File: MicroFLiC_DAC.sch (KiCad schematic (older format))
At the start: 35 parts, among them P1 2x4_MicroMaTch, P2 2x4_HEADER, P3 SMA, P4 SMA, P5 SMA, P6 SMA, P7 1x2_HEADER, P8 1x2_SOCKET, U1 DAC8734

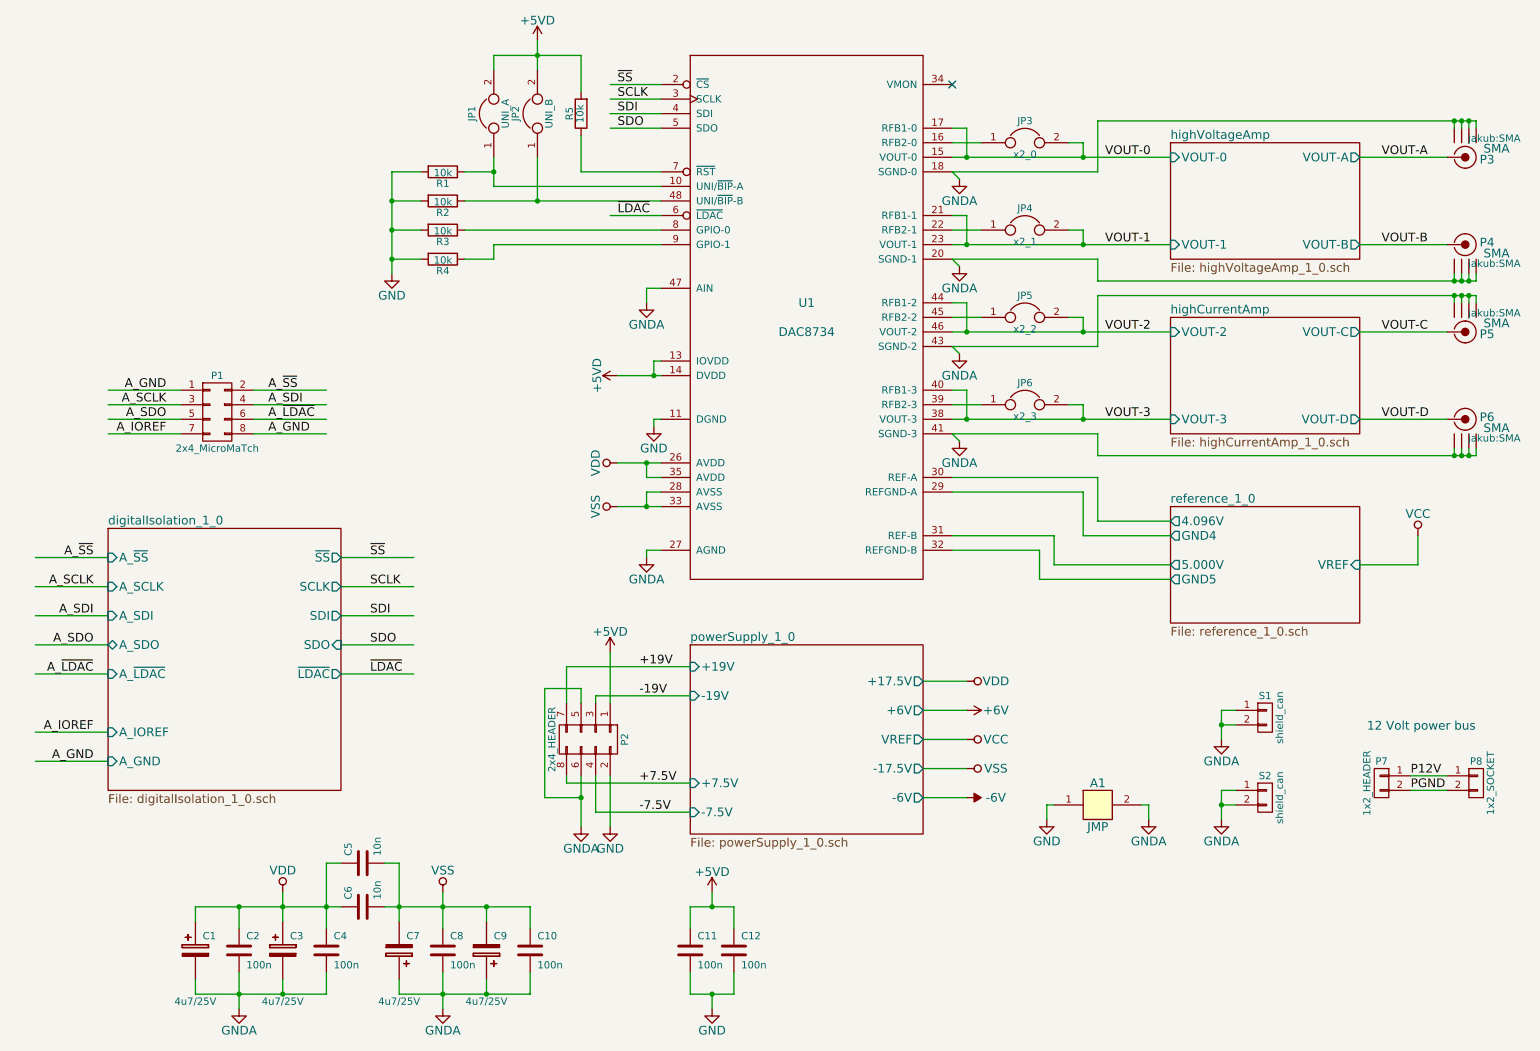
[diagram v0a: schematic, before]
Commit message: Updated all part descriptions
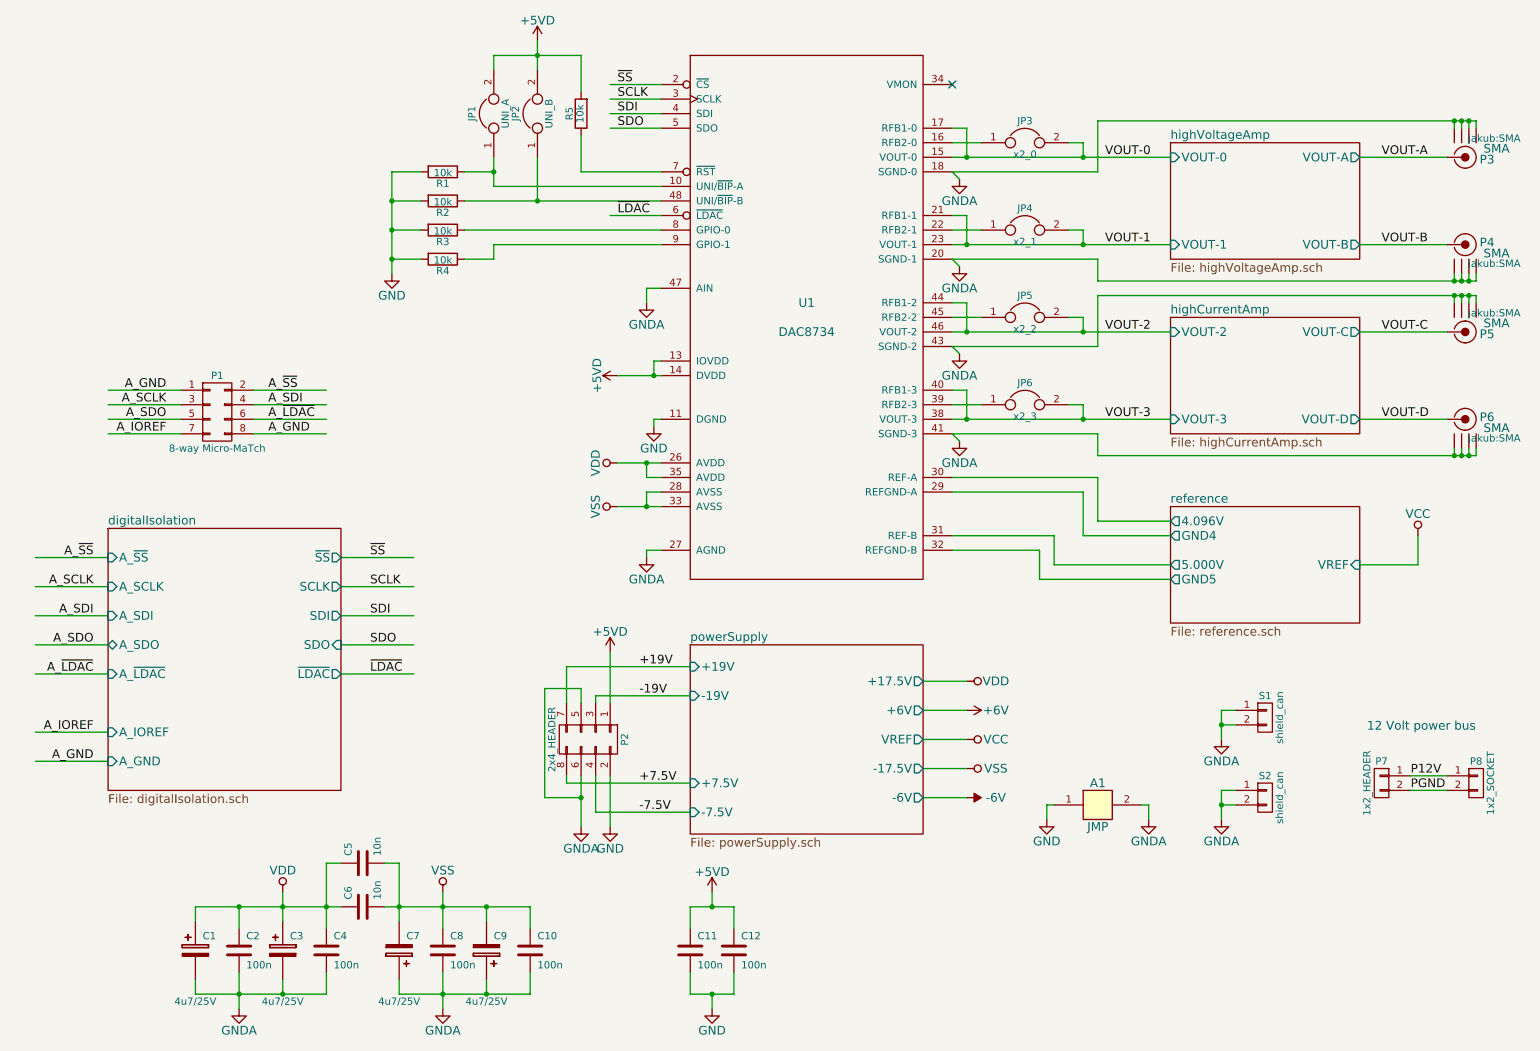
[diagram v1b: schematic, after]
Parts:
- C1, C3, C7, C9: Alt. Order Code (none) -> 74-TR3B475K025C0700; Alt. Supplier (none) -> Mouser; Note (none) -> 4.7μF/25V/0.7Ω ESR case B tantalum capacitor; Package (none) -> case B; Supplier (none) -> Farnell
- C10, C11, C12, C2, C4, C8: Alt. Order Code (none) -> 710-885012206095; Alt. Supplier (none) -> Mouser; Note (none) -> 100nF/50V X7R 0603 ceramic capacitor; Package (none) -> 0603; Supplier (none) -> Farnell
- C5, C6: Alt. Order Code (none) -> 77-VJ0603Y103KXACBC; Alt. Supplier (none) -> Mouser; Note (none) -> 10nF/100V X7R 0603 ceramic capacitor; Package (none) -> 0603; Supplier (none) -> Farnell
- P1: value 2x4_MicroMaTch -> 8-way Micro-MaTch; Alt. Order Code (none) -> 571-7-188275-8; Alt. Supplier (none) -> Mouser; Note (none) -> 8-way SMD Micro-MaTch connector; Package (none) -> Micro-MaTch SMD; Supplier (none) -> Farnell
- P2: Alt. Order Code (none) -> 710-61300421121; Alt. Supplier (none) -> Mouser; Note (none) -> 2x4 header strip; Package (none) -> DIL-8; Supplier (none) -> Farnell
- P3, P4, P5, P6: Alt. Order Code (none) -> 538-73251-2200; Alt. Supplier (none) -> Mouser; Note (none) -> R/A SMA jack; Package (none) -> SMA; Supplier (none) -> Farnell
- P7: Alt. Order Code (none) -> 855-M20-9990245; Alt. Supplier (none) -> Mouser; Note (none) -> 1x2 header strip; Package (none) -> SIL-2; Supplier (none) -> Farnell
- P8: Alt. Order Code (none) -> ESQ-102-33-G-S; Alt. Supplier (none) -> Samtec; Note (none) -> 1x2 ESQ series elevated socket strip; Package (none) -> SIL-2; Part Number SSA-102-S-G -> ESQ-102-33-G-S; Supplier (none) -> Farnell
- R1, R2, R3, R4, R5: Alt. Order Code (none) -> 71-CRCW0805-10K-E3; Alt. Supplier (none) -> Mouser; Note (none) -> 10kΩ/1% 0805 resistor; Package (none) -> 0805; Supplier (none) -> Farnell
- S1, S2: Alt. Order Code (none) -> MS323-20; Alt. Supplier (none) -> Masach; Note (none) -> Two-piece EMI shielding can; Order Code 826-6788 (RS Components) -> 826-6788; Package (none) -> Can; Supplier (none) -> RS Components
- U1: Alt. Order Code (none) -> 595-DAC8734SPFB; Alt. Supplier (none) -> Mouser; Note (none) -> Quad 16-bit DAC; Package (none) -> TQFP-48; Supplier (none) -> Farnell

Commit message: Fixed P8 socket Farnell code
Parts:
- P8: Order Code 1668221 -> 1927389
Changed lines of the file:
@@
 F 6 "SIL-2" H 10700 5850 60  0001 C CNN "Package"
 F 7 "Farnell" H 10700 5850 60  0001 C CNN "Supplier"
-F 8 "1668221" H 10700 5850 60  0001 C CNN "Order Code"
+F 8 "1927389" H 10700 5850 60  0001 C CNN "Order Code"
 F 9 "Samtec" H 10700 5850 60  0001 C CNN "Alt. Supplier"
 F 10 "ESQ-102-33-G-S" H 10700 5850 60  0001 C CNN "Alt. Order Code"

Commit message: Fixed P2 socket Farnell code
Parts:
- P2: Alt. Order Code 710-61300421121 -> 855-M20-9980446; Manufacturer Wurth Elektronik -> Harwin; Order Code 2356130 -> 1022233; Part Number 61300421121 -> M20-9980446
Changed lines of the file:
@@
 F 2 "Pin_Headers:Pin_Header_Straight_2x04" H 4600 4350 60  0001 C CNN
 F 3 "" H 4600 4350 60  0000 C CNN
-F 4 "61300421121" H 4600 5550 60  0001 C CNN "Part Number"
-F 5 "Wurth Elektronik" H 4600 5550 60  0001 C CNN "Manufacturer"
+F 4 "M20-9980446" H 4600 5550 60  0001 C CNN "Part Number"
+F 5 "Harwin" H 4600 5550 60  0001 C CNN "Manufacturer"
 F 6 "DIL-8" H 4600 5550 60  0001 C CNN "Package"
 F 7 "Farnell" H 4600 5550 60  0001 C CNN "Supplier"
-F 8 "2356130" H 4600 5550 60  0001 C CNN "Order Code"
+F 8 "1022233" H 4600 5550 60  0001 C CNN "Order Code"
 F 9 "Mouser" H 4600 5550 60  0001 C CNN "Alt. Supplier"
-F 10 "710-61300421121" H 4600 5550 60  0001 C CNN "Alt. Order Code"
+F 10 "855-M20-9980446" H 4600 5550 60  0001 C CNN "Alt. Order Code"
 F 11 "2x4 header strip" H 4600 5550 60  0001 C CNN "Note"
 	1    4600 5550

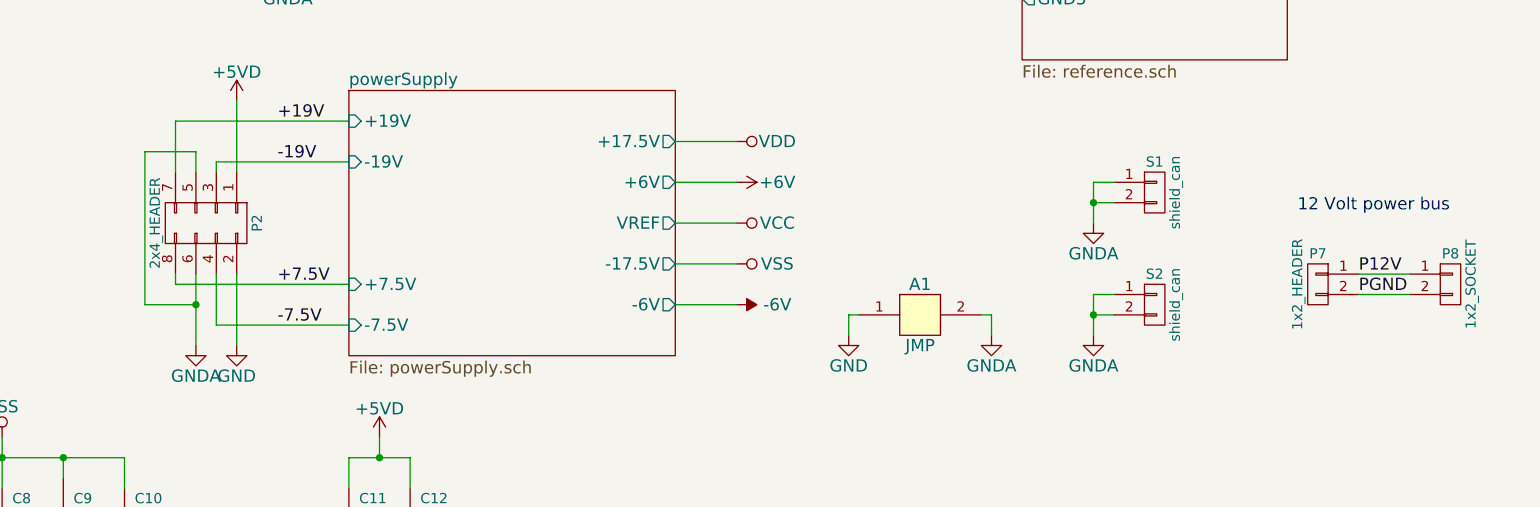
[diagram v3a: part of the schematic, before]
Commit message: Fixed connector descriptions
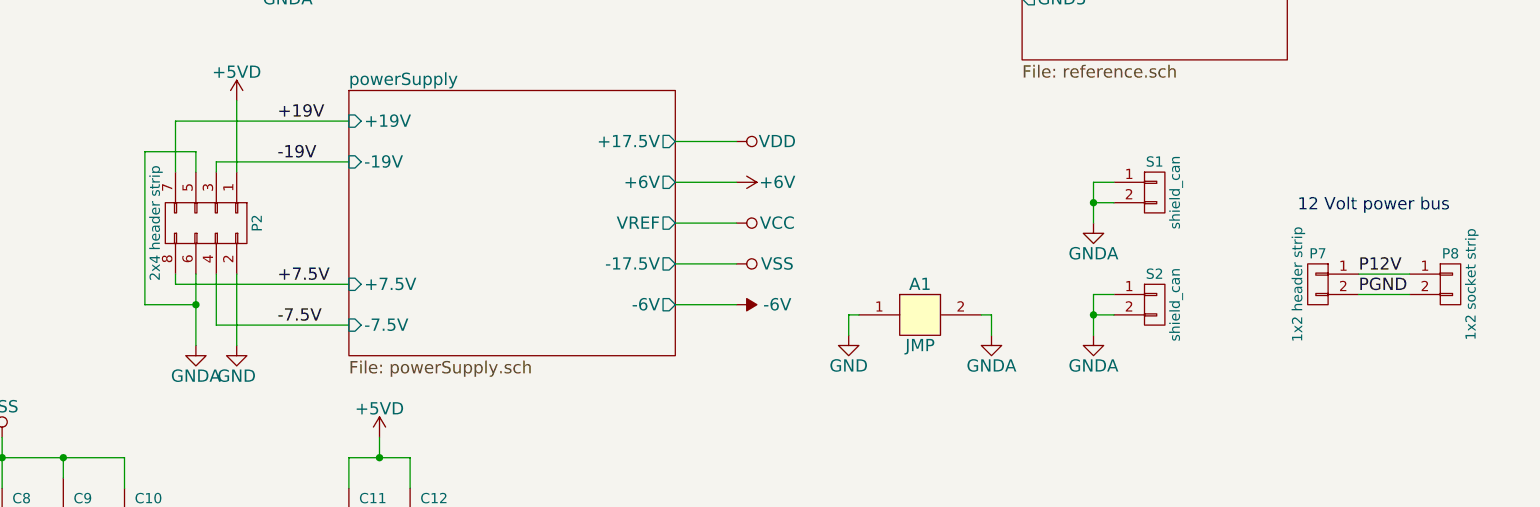
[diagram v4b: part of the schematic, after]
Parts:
- P2: value 2x4_HEADER -> 2x4 header strip
- P7: value 1x2_HEADER -> 1x2 header strip
- P8: value 1x2_SOCKET -> 1x2 socket strip
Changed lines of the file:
@@
 P 10700 5850
 F 0 "P8" H 10700 6000 50  0000 C CNN
-F 1 "1x2_SOCKET" V 10800 5850 50  0000 C CNN
+F 1 "1x2 socket strip" V 10800 5850 50  0000 C CNN
 F 2 "Socket_Strips:Socket_Strip_Straight_1x02" H 10700 5850 60  0001 C CNN
 F 3 "" H 10700 5850 60  0000 C CNN
@@
 P 10050 5850
 F 0 "P7" H 10050 6000 50  0000 C CNN
-F 1 "1x2_HEADER" V 10150 5850 50  0000 C CNN
+F 1 "1x2 header strip" V 10150 5850 50  0000 C CNN
 F 2 "Pin_Headers:Pin_Header_Straight_1x02" H 10050 5850 60  0001 C CNN
 F 3 "" H 10050 5850 60  0000 C CNN
@@
 P 4600 5550
 F 0 "P2" H 4600 5800 50  0000 C CNN
-F 1 "2x4_HEADER" H 4600 5300 50  0000 C CNN
+F 1 "2x4 header strip" H 4600 5300 50  0000 C CNN
 F 2 "Pin_Headers:Pin_Header_Straight_2x04" H 4600 4350 60  0001 C CNN
 F 3 "" H 4600 4350 60  0000 C CNN

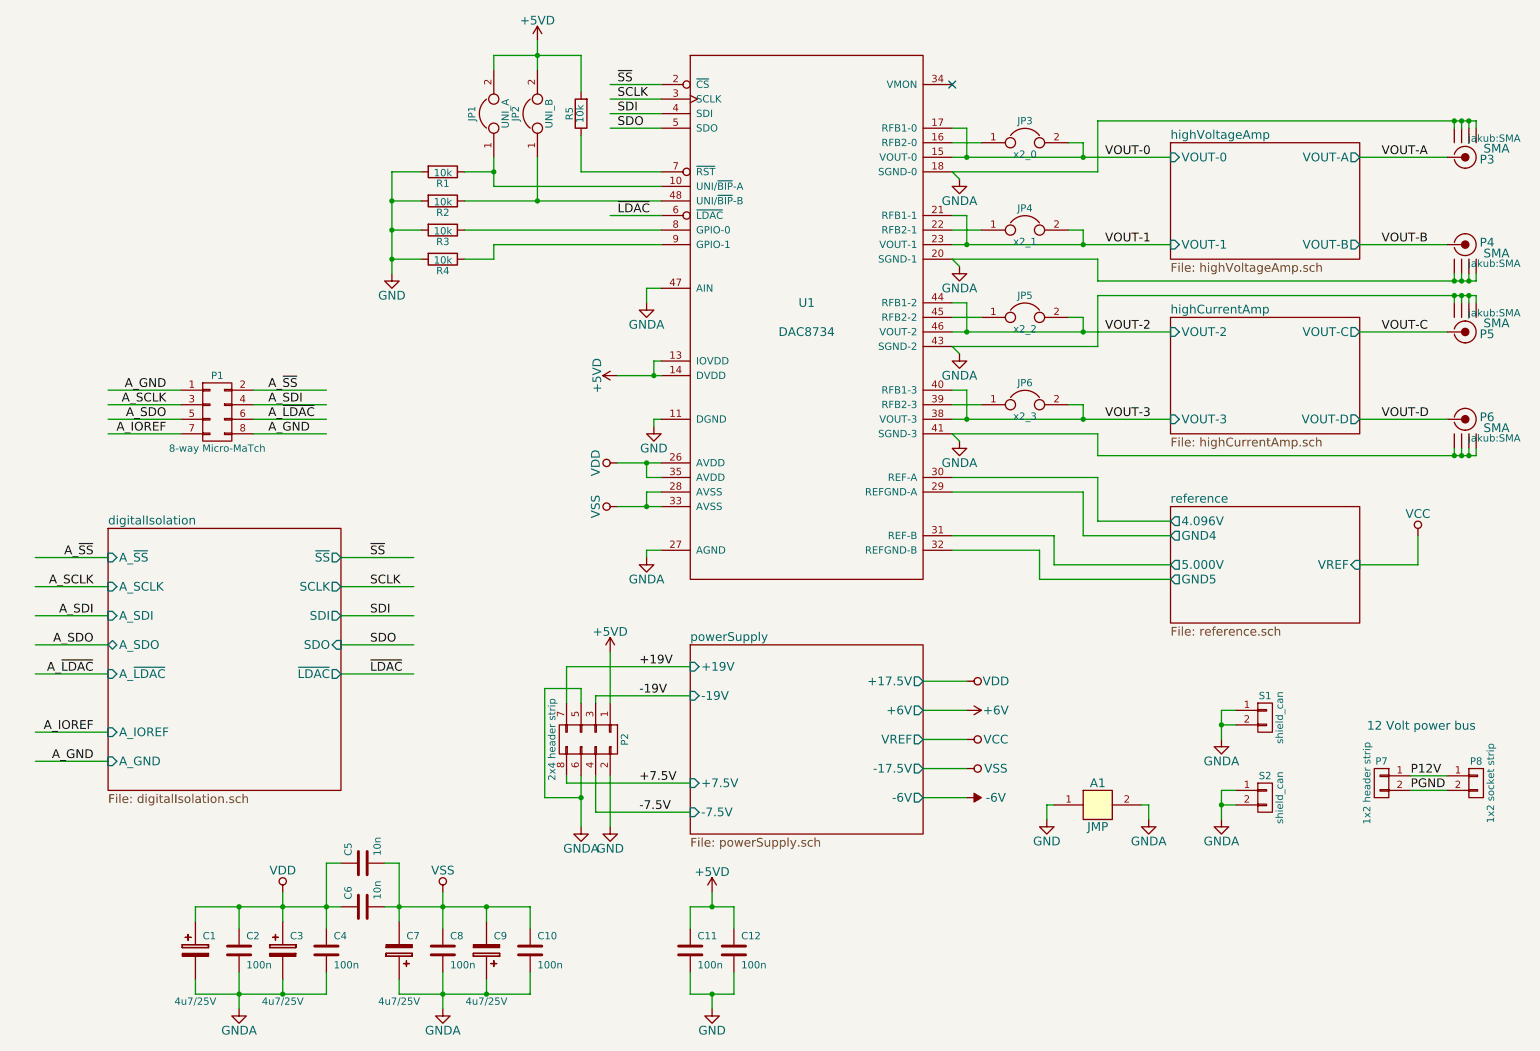
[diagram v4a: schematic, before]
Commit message: Fixed ground problems, added bypass capacitors, added resistor between digital isolator and DAC
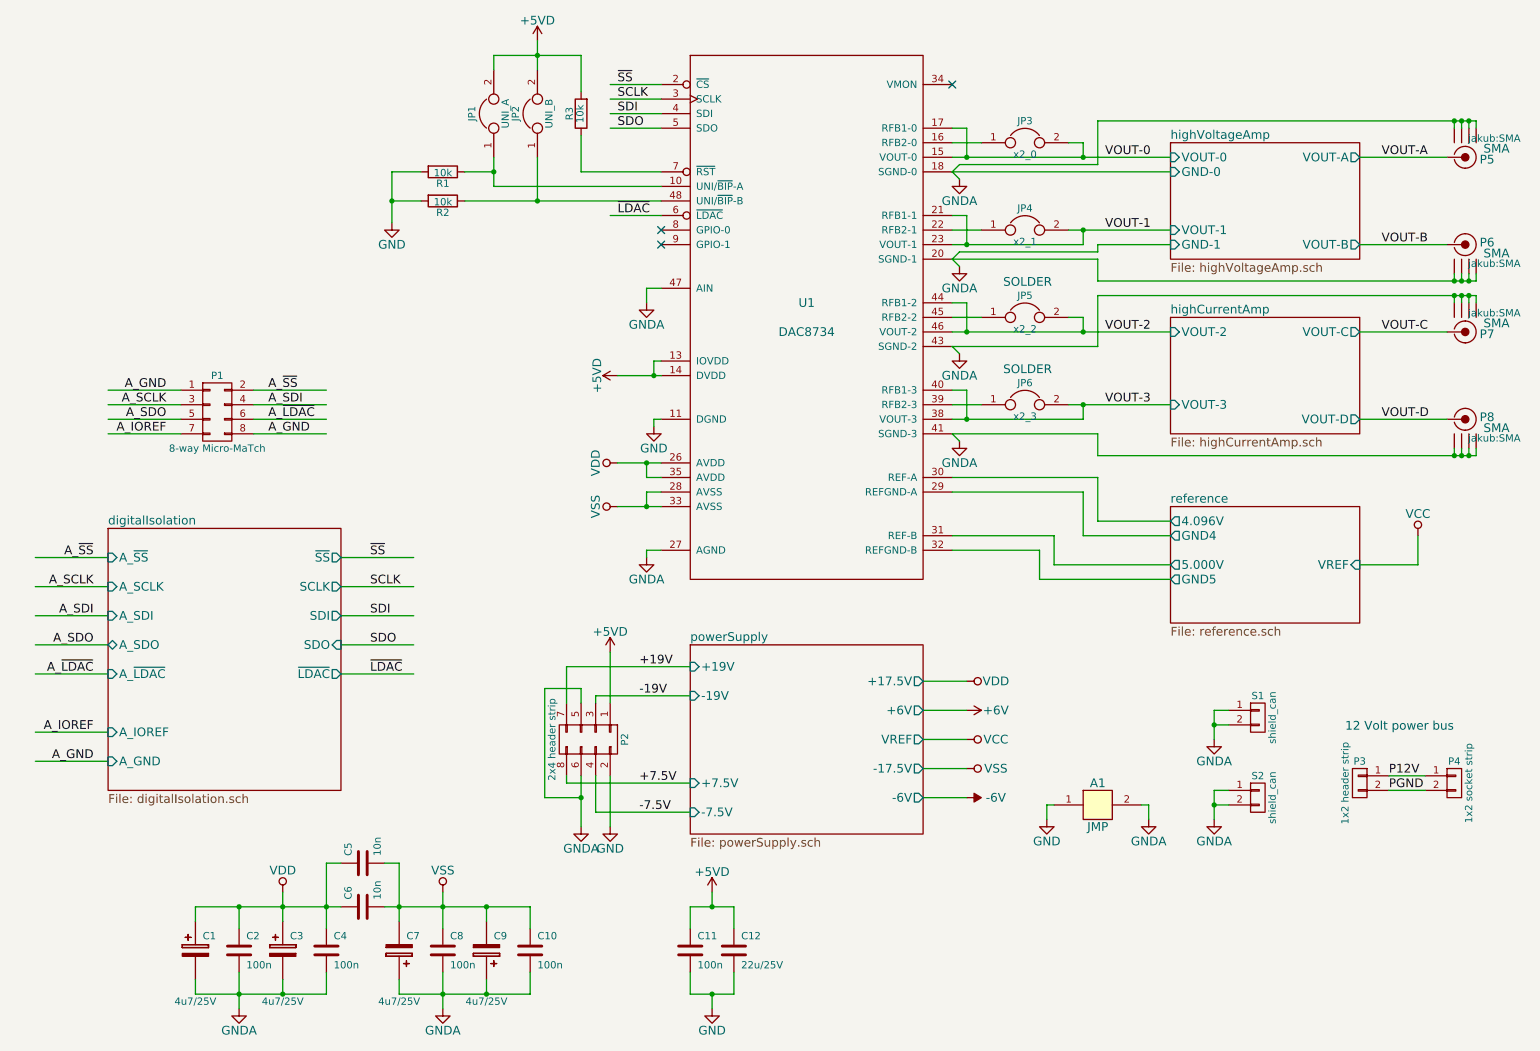
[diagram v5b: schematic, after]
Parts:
- removed R3, R4: 10k, Resistors_SMD:R_0805, symbol R
- C12: value 100n -> 22u/25V; footprint Capacitors_SMD:C_0603 -> Capacitors_SMD:C_1210; Alt. Order Code 710-885012206095 -> 81-GRM32ER61E226ME5L; Manufacturer Multicomp -> Murata; Note 100nF/50V X7R 0603 ceramic capacitor -> 22μF/25V X5R 1210 ceramic capacitor; Order Code 1759122 -> 1735539; Package 0603 -> 1210; Part Number MC0603B104K500CT -> GRM32ER61E226ME15L
- renumbered P7 to P3, P8 to P4, P3 to P5, P4 to P6, P5 to P7, P6 to P8, R5 to R3
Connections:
- no-connect marks 1 -> 3
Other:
- note added: "SOLDER"
- moved on the sheet: P3, P4, S1, S2
